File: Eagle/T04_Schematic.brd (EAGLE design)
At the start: 40.6 x 63.5 mm, 29 parts

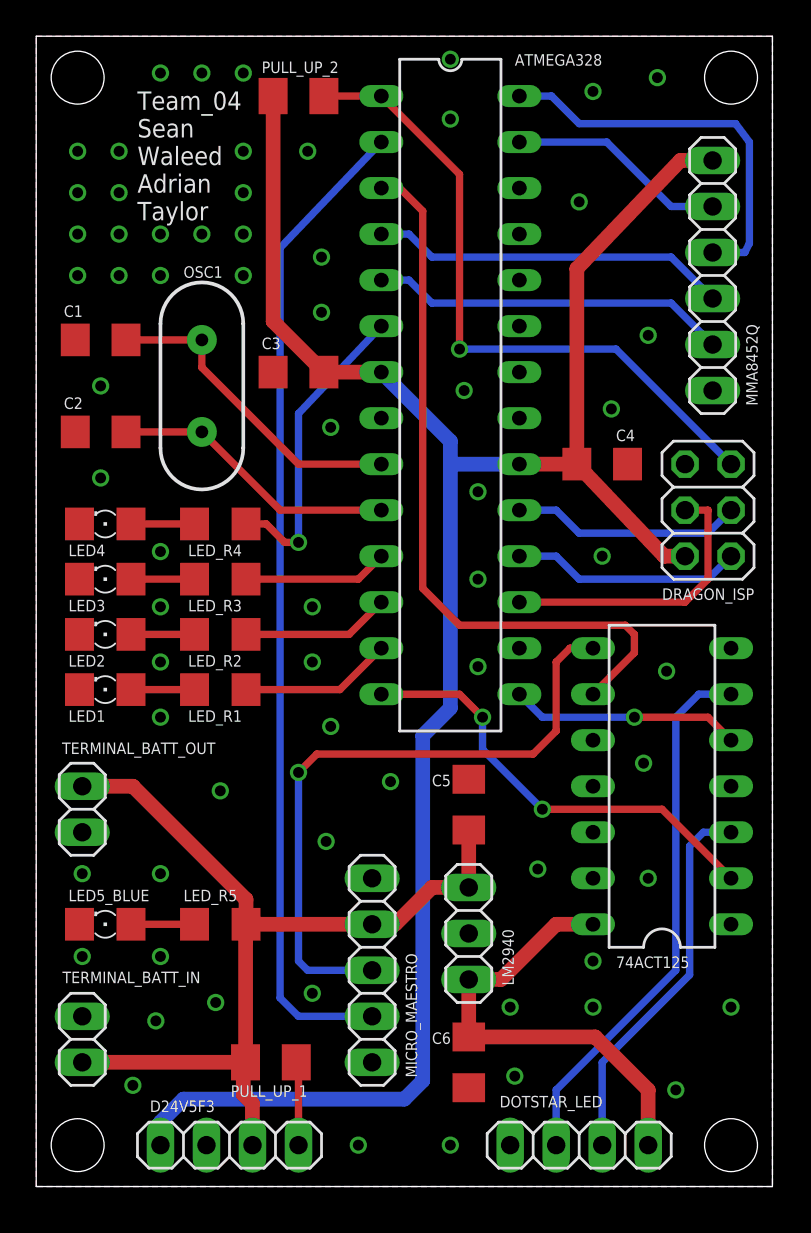
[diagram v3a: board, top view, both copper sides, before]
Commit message: Added Andrew's Changes and Some more Silk Screen ID
Hi Taylor,

> We've been getting great feedback from you on our schematic/layout and
I
> was wondering if you could take one last look at our layout to see if
we
> missed anything major before we submit it.

I didn't have much time to look, but here you go:

Schematic:

- IMPORTANT: Chip "74ACT125" has an uninvoked gate. It's a quad buffer
part, and one of the buffers isn't hooked up. Use the INVOKE command in
eagle and click on that part to get the fourth buffer. Tie the input and
the enable line to low/high as you see fit -- but don't leave it
floating, like it is now.

- IMPORTANT: Chip "74ACT125" needs aq bypass cap.

- NOT IMPORTANT: Usually schematics have part identifiers that have
non-semantic meanings: like R1, R2, R3 not "PULL_UP_1". This is because
things move around a lot, and it's easier to type, and not get mixed up.
That said, I don't really care, feel free to leave it that way. But in
general, with schematics you share with others, I'd stick with regular
part identifiers.

Layout:

- MAYBE IMPORTANT: your ISP connector is a little close to the chip
below it and conector above. I think you'll be OK, but I'm not sure -
you might want to move that other connector a bit up away from the ISP
connector. But if you've printed it out and it looks OK, ignore this.

- NOT IMPORTANT: your board mounting holes are 0.115 inches, which is a
REALLY tight fit for a #4 screw. You might want to open it up to 0.125
if you have room.

- Otherwise: Looks great!
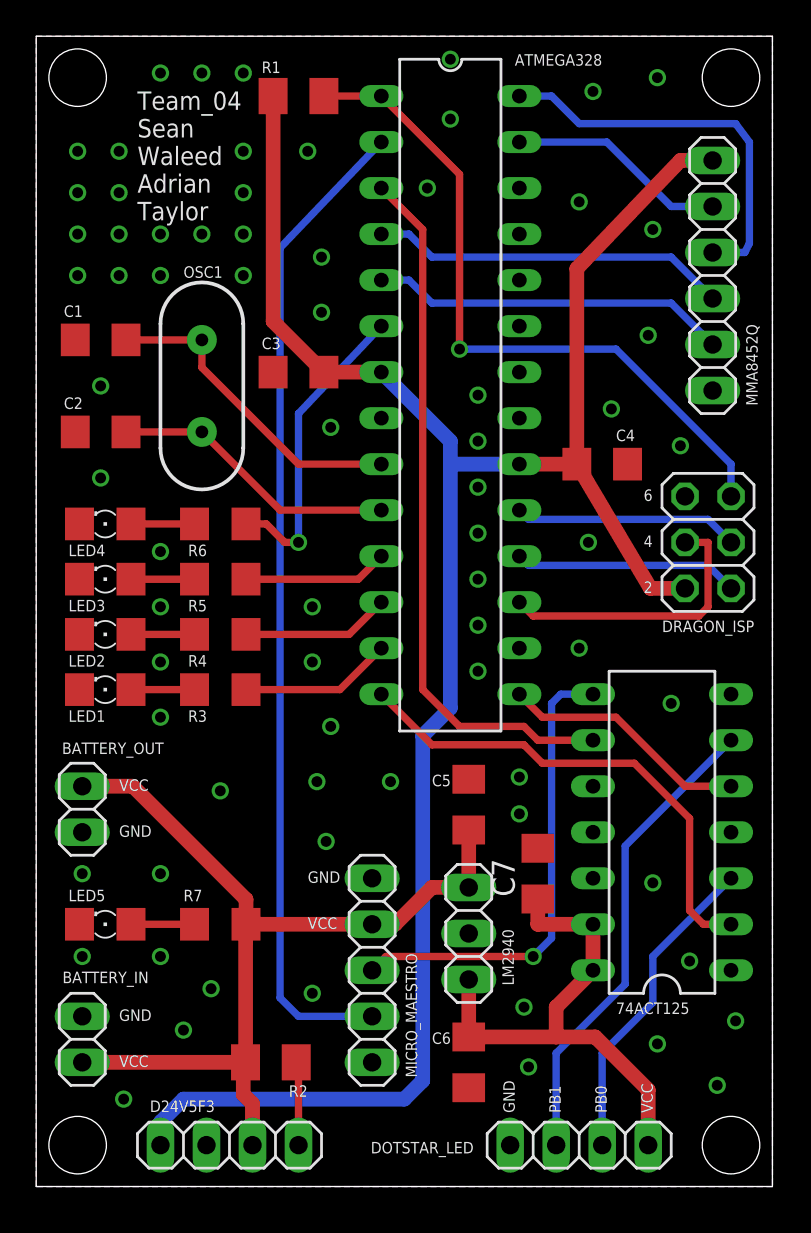
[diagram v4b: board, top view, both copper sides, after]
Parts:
- added C7: 100 nF, rcl:C1206
- moved 74ACT125 2.54 mm to (34.5, 19.6)
- moved DRAGON_ISP 1.78 mm to (37.1, 35.6)
- renumbered LED5_BLUE to LED5, LED_R1 to R3, LED_R2 to R4, LED_R3 to R5, LED_R4 to R6, LED_R5 to R7, PULL_UP_1 to R2, PULL_UP_2 to R1, TERMINAL_BATT_IN to BATTERY_IN, TERMINAL_BATT_OUT to BATTERY_OUT
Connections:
- net 5V_VCC: now also 74ACT125.13, C7.1
- net GND: now also 74ACT125.11, 74ACT125.12, C7.2
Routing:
- net RXD: track 36.0 -> 26.1 mm
- net N$13: track 29.9 -> 26.3 mm
- net N$8: track 21.1 -> 17.7 mm
- net 5V_VCC: track 25.5 -> 28.8 mm
- net CLOCK: track 24.6 -> 27.5 mm, vias 2 -> 0
- net RESET: track 36.5 -> 38.3 mm
- net VCC: track 113.6 -> 115.3 mm
- net UP_TXD: track 40.6 -> 39.2 mm
- net DATA: track 12.7 -> 13.8 mm, vias 1 -> 0
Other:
- board text added: "2"
- board text added: "4"
- board text added: "6"
- board text added: "GND"
- board text added: "PB0"
- board text added: "PB1"
- board text added: "VCC"
